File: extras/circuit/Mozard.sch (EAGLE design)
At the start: 44 parts, among them J4 Headphone/Line Out, U2 LM386

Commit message: Updated
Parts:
- C1: value 4.7nF -> 4.7nF/472
- C2: value 10uF -> 10uF/106
- C4: value 100nF -> 100nF/104
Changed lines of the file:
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@@
 <?xml version="1.0" encoding="utf-8"?>
 <!DOCTYPE eagle SYSTEM "eagle.dtd">
-<eagle version="9.1.1">
+<eagle version="9.1.3">
 <drawing>
 <settings>
@@
 <part name="VOLUME" library="SparkFun-Electromechanical" deviceset="POT" device="ALPS-KIT" value="VOLUME"/>
 <part name="R4" library="adafruit" deviceset="R-US_" device="0204/7" value="270"/>
-<part name="C4" library="SparkFun-Capacitors" deviceset="0.1UF-50V-20%(PTH)" device="KIT-EZ" value="100nF"/>
+<part name="C4" library="SparkFun-Capacitors" deviceset="0.1UF-50V-20%(PTH)" device="KIT-EZ" value="100nF/104"/>
 <part name="GND2" library="SparkFun-Aesthetics" deviceset="GND" device=""/>
 <part name="A7" library="SparkFun-Electromechanical" deviceset="POT" device="ALPS-KIT" value="A7"/>
@@
 <part name="P+1" library="supply1" library_urn="urn:adsk.eagle:library:371" deviceset="V+" device=""/>
 <part name="U$1" library="TOF" deviceset="NANO" device=""/>
-<part name="C1" library="SparkFun-Capacitors" deviceset="0.1UF-50V-20%(PTH)" device="KIT-EZ" value="4.7nF"/>
-<part name="C2" library="SparkFun-Capacitors" deviceset="0.1UF-50V-20%(PTH)" device="KIT-EZ" value="10uF"/>
+<part name="C1" library="SparkFun-Capacitors" deviceset="0.1UF-50V-20%(PTH)" device="KIT-EZ" value="4.7nF/472"/>
+<part name="C2" library="SparkFun-Capacitors" deviceset="0.1UF-50V-20%(PTH)" device="KIT-EZ" value="10uF/106"/>
 <part name="TOUCH1" library="TOF" deviceset="PCB-TOUCHPAD2" device=""/>
 <part name="GND3" library="SparkFun-Aesthetics" deviceset="GND" device=""/>

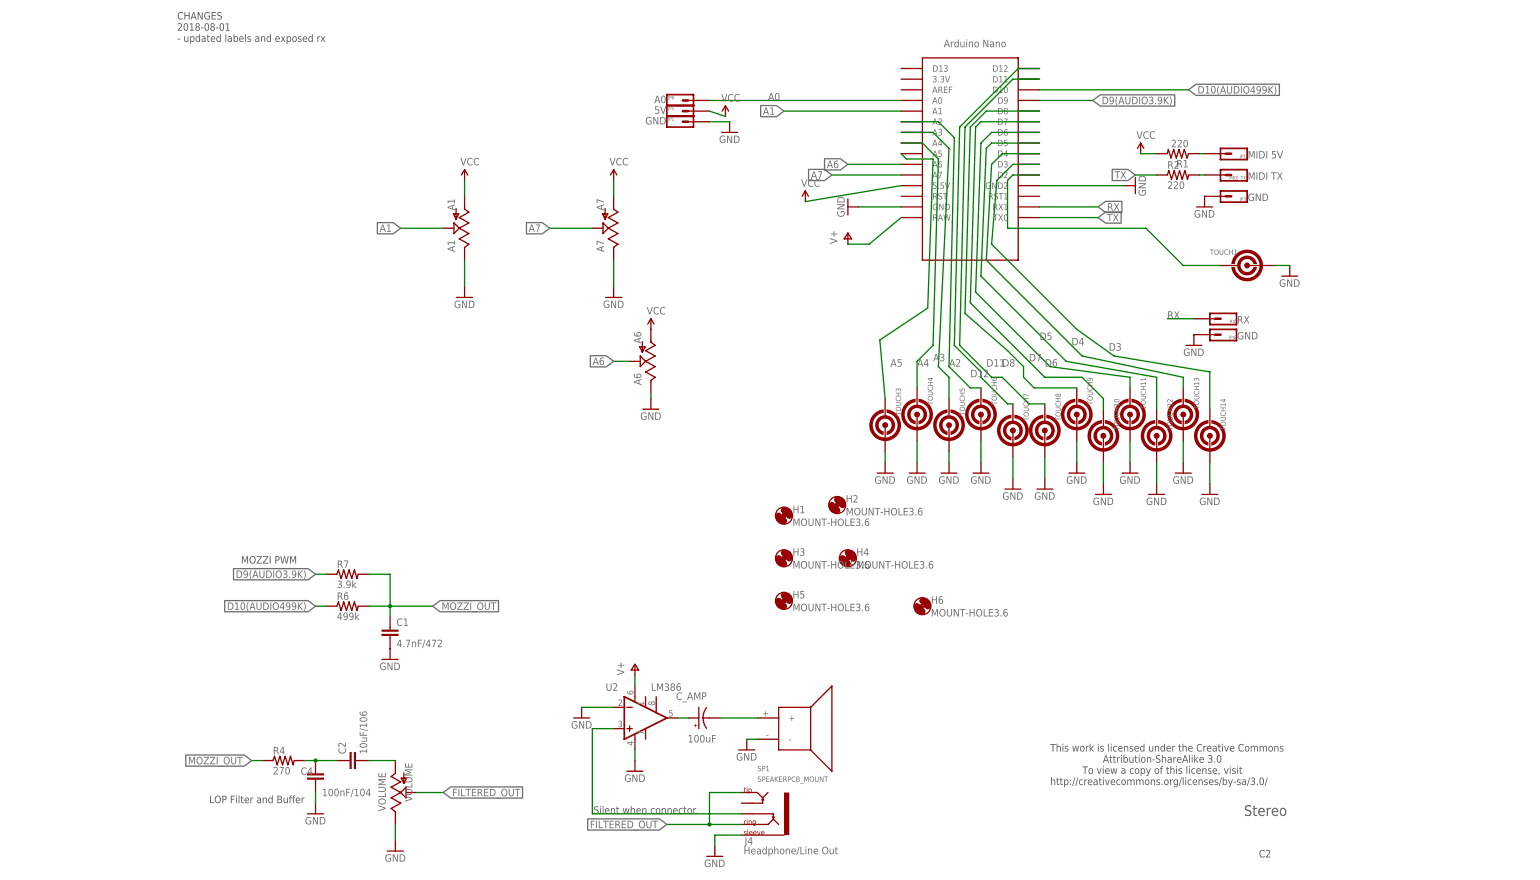
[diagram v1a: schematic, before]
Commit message: Fixed overlapping traces
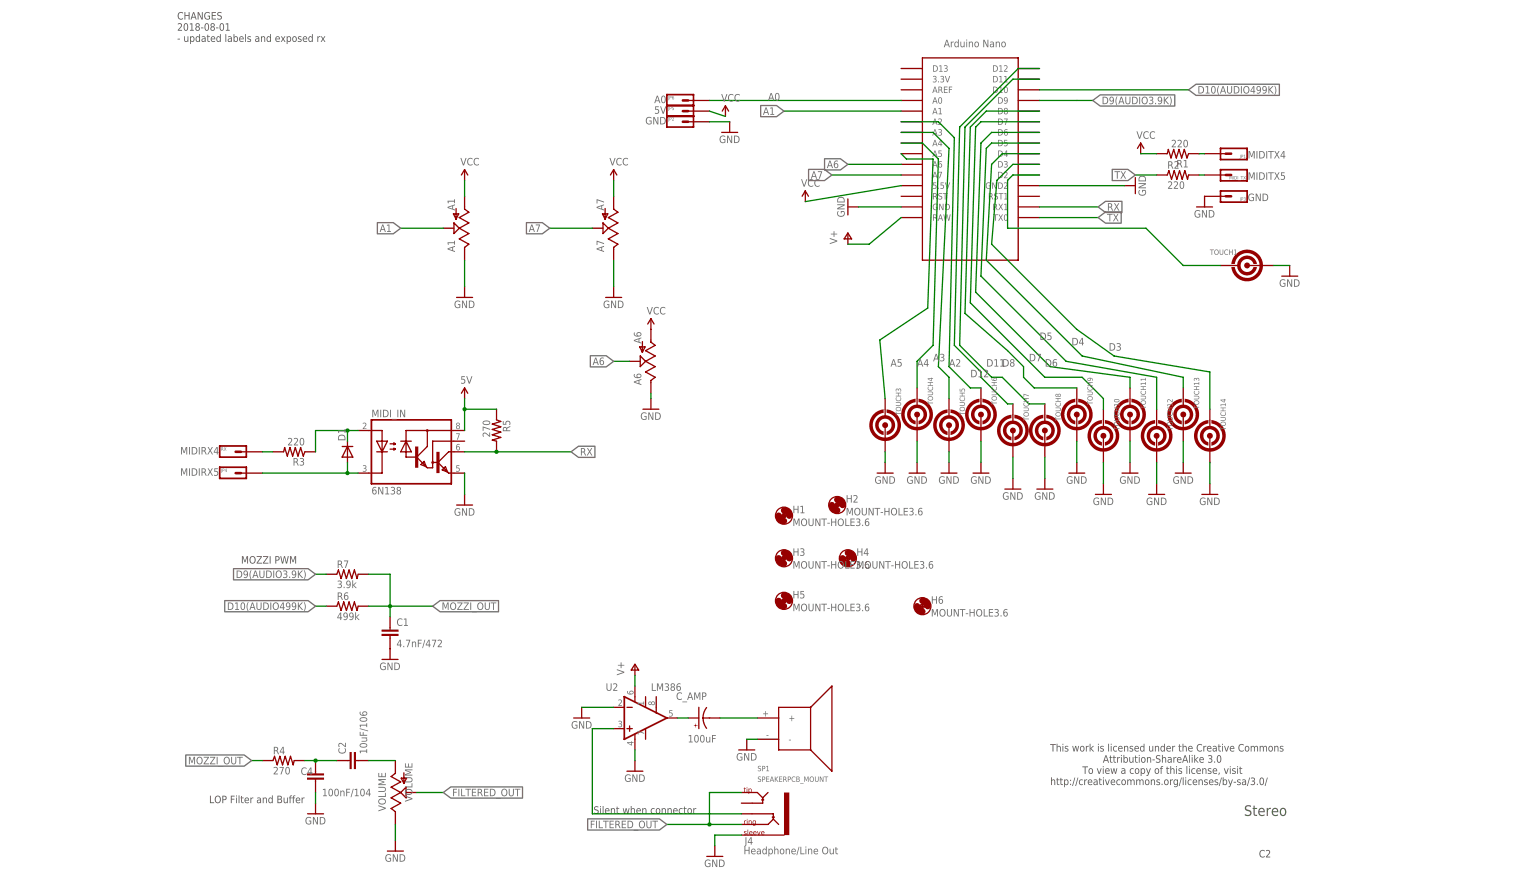
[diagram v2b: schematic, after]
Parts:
- added D1: 1N4148, adafruit:1N4004
- added MIDI_IN: 6N138, optocoupler:6N138
- added R3: 220, adafruit:R-US_0204/5
- added R5: 270, adafruit:R-US_0204/5
- JP1: value MIDI 5V -> MIDITX4
- JP4: value GND -> MIDIRX5
- MIDI_TX: value MIDI TX -> MIDITX5
- R1, R2: device adafruit:R-US_0204/7 -> adafruit:R-US_0204/5
- RX: value RX -> MIDIRX4
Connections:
- new net 5V: MIDI_IN.VCC, R5.1
- new net N$10: D1.C, MIDI_IN.A, R3.1
- new net N$8: D1.A, JP4.1, MIDI_IN.C
- new net N$9: R3.2, RX.1
- net GND: now also MIDI_IN.GND; no longer JP4.1
- net RX: now also MIDI_IN.VO, R5.2; no longer RX.1
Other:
- moved on the sheet: JP4, RX

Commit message: Sensitivity change
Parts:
- removed JP1: MIDITX4, TOF:HEADER-1X1
- removed JP3: GND, TOF:HEADER-1X1
- removed JP4: MIDIRX5, TOF:HEADER-1X1
- removed MIDI_TX: MIDITX5, TOF:HEADER-1X1
- removed R1, R2: 220, adafruit:R-US_0204/5
- removed RX: MIDIRX4, TOF:HEADER-1X1
- removed TOUCH1, TOUCH10, TOUCH11, TOUCH12, TOUCH13, TOUCH14, TOUCH3, TOUCH4, TOUCH5, TOUCH6, TOUCH7, TOUCH8, TOUCH9: (no value), TOF:PCB-TOUCHPAD2
- added MIDI_IN1: AUDIO-JACKKIT, TOF:AUDIO-JACKKIT
- added U$10, U$11, U$12, U$13, U$14, U$2, U$3, U$4, U$5, U$6, U$7, U$8, U$9: PCB-TOUCHPAD-1-PIN, TOF:PCB-TOUCHPAD-1-PIN
- A1, A6, A7, VOLUME: device SparkFun-Electromechanical:POTALPS-KIT -> TOF:POT
- D1: device adafruit:1N4004 -> TOF:DIODE
- MIDI_IN: device optocoupler:6N138 -> TOF:6N138
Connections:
- removed net N$3: JP1.1, R1.1
- removed net N$5: MIDI_TX.1, R2.2
- removed net N$8: D1.A, JP4.1, MIDI_IN.C
- removed net N$9: R3.2, RX.1
- new net M4: MIDI_IN1.RING, R3.2
- new net M5: D1.A, MIDI_IN.C, MIDI_IN1.TIP
- net A2: now also U$5.P$1; no longer TOUCH6.1
- net A3: now also U$4.P$1; no longer TOUCH5.1
- net A4: now also U$3.P$1; no longer TOUCH4.1
- net A5: now also U$2.P$1; no longer TOUCH3.1
- net D11: now also U$7.P$1; no longer TOUCH8.1
- net D12: now also U$6.P$1; no longer TOUCH7.1
- net D3: now also U$13.P$1; no longer TOUCH14.1
- net D4: now also U$12.P$1; no longer TOUCH13.1
- net D5: now also U$11.P$1; no longer TOUCH12.1
- net D6: now also U$10.P$1; no longer TOUCH11.1
- net D7: now also U$9.P$1; no longer TOUCH10.1
- net D8: now also U$8.P$1; no longer TOUCH9.1
- net GND: now also MIDI_IN1.SLEEVE; no longer JP3.1, TOUCH1.2, TOUCH10.2, TOUCH11.2, TOUCH12.2, TOUCH13.2, TOUCH14.2, TOUCH3.2, TOUCH4.2, TOUCH5.2, TOUCH6.2, TOUCH7.2, TOUCH8.2, TOUCH9.2
- net TOUCH_A: now also U$14.P$1; no longer TOUCH1.1
- net TX: no longer R2.1
- net VCC: no longer R1.2

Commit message: Cap removed, resistor added
Big capacitor removed because it was useless. 100k resistor added between + and - of amp to cancel noise when jack plugged in.
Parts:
- added R1: 100k, adafruit:R-US_0204/7
- C_AMP: device Mitch-parts:CPOL-RADIAL-10UF-25V -> TOF:CPOL-USE2.5-6
- SP1: value SPEAKERPCB_MOUNT -> SPEAKER
- renumbered D1 to 1N4148
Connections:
- net GND: now also R1.2
- net N$6: now also R1.1
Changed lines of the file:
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@@
 <setting verticaltext="up"/>
 </settings>
-<grid distance="0.1" unitdist="inch" unit="inch" style="lines" multiple="1" display="no" altdistance="0.025" altunitdist="inch" altunit="inch"/>
+<grid distance="0.1" unitdist="inch" unit="inch" style="lines" multiple="1" display="no" altdistance="0.01" altunitdist="inch" altunit="inch"/>
 <layers>
 <layer number="1" name="Top" color="4" fill="1" visible="no" active="no"/>
@@
 <part name="GND14" library="SparkFun-Aesthetics" deviceset="GND" device=""/>
 <part name="U2" library="Mitch-parts" deviceset="LM386" device=""/>
-<part name="C_AMP" library="Mitch-parts" deviceset="CPOL-RADIAL-10UF-25V" device="" value="100uF"/>
+<part name="C_AMP" library="TOF" deviceset="CPOL-US" device="E2.5-6" package3d_urn="urn:adsk.eagle:package:23349/1" value="100uF"/>
 <part name="P+1" library="supply1" library_urn="urn:adsk.eagle:library:371" deviceset="V+" device=""/>
 <part name="U$1" library="TOF" deviceset="NANO" device=""/>
@@
 <part name="H5" library="holes" library_urn="urn:adsk.eagle:library:237" deviceset="MOUNT-HOLE" device="3.6" package3d_urn="urn:adsk.eagle:package:14272/1"/>
 <part name="H6" library="holes" library_urn="urn:adsk.eagle:library:237" deviceset="MOUNT-HOLE" device="3.6" package3d_urn="urn:adsk.eagle:package:14272/1"/>
-<part name="SP1" library="SparkFun-Electromechanical" deviceset="SPEAKER" device="" technology="PCB_MOUNT"/>
+<part name="SP1" library="SparkFun-Electromechanical" deviceset="SPEAKER" device="" technology="PCB_MOUNT" value="SPEAKER"/>
 <part name="JP2" library="TOF" deviceset="HEADER-1X1" device="" value="GND"/>
 <part name="JP5" library="TOF" deviceset="HEADER-1X1" device="" value="5V"/>
@@
 <part name="SUPPLY5" library="SparkFun-Aesthetics" deviceset="VCC" device=""/>
 <part name="MIDI_IN" library="TOF" deviceset="6N138" device="" package3d_urn="urn:adsk.eagle:package:21941/1"/>
-<part name="D1" library="TOF" deviceset="DIODE" device="" value="1N4148"/>
+<part name="1N4148" library="TOF" deviceset="DIODE" device="" value="1N4148"/>
 <part name="R3" library="adafruit" deviceset="R-US_" device="0204/5" value="220"/>
 <part name="GND29" library="SparkFun-Aesthetics" deviceset="GND" device=""/>
@@
 <part name="U$13" library="TOF" deviceset="PCB-TOUCHPAD-1-PIN" device=""/>
 <part name="U$14" library="TOF" deviceset="PCB-TOUCHPAD-1-PIN" device=""/>
+<part name="R1" library="adafruit" deviceset="R-US_" device="0204/7" value="100k"/>
 </parts>
 <sheets>
@@
 <attribute name="VALUE" x="169.672" y="76.2762" size="1.778" layer="96"/>
 </instance>
-<instance part="GND4" gate="1" x="104.14" y="40.64" smashed="yes">
-<attribute name="VALUE" x="101.6" y="38.1" size="1.778" layer="96"/>
+<instance part="GND4" gate="1" x="88.9" y="40.64" smashed="yes">
+<attribute name="VALUE" x="86.36" y="38.1" size="1.778" layer="96"/>
 </instance>
 <instance part="GND14" gate="1" x="116.84" y="27.94" smashed="yes">
@@
 <attribute name="VALUE" x="53.975" y="93.98" size="1.778" layer="96"/>
 </instance>
-<instance part="D1" gate="1" x="48.26" y="104.14" smashed="yes" rot="R90">
+<instance part="1N4148" gate="1" x="48.26" y="104.14" smashed="yes" rot="R90">
 <attribute name="NAME" x="47.7774" y="106.68" size="1.778" layer="95" rot="R90"/>
 </instance>
@@
 <instance part="U$13" gate="G$1" x="254" y="106.68" smashed="yes" rot="R270"/>
 <instance part="U$14" gate="G$1" x="264.16" y="148.59" smashed="yes"/>
+<instance part="R1" gate="G$1" x="100.33" y="38.1" smashed="yes" rot="R90">
+<attribute name="NAME" x="98.8314" y="35.56" size="1.778" layer="95" rot="R90"/>
+<attribute name="VALUE" x="103.632" y="35.56" size="1.778" layer="96" rot="R90"/>
+</instance>
 </instances>
 <busses>
@@
 <segment>
 <pinref part="GND4" gate="1" pin="GND"/>
-<wire x1="111.76" y1="43.18" x2="104.14" y2="43.18" width="0.1524" layer="91"/>
+<wire x1="111.76" y1="43.18" x2="100.33" y2="43.18" width="0.1524" layer="91"/>
 <pinref part="U2" gate="G$1" pin="-IN"/>
+<pinref part="R1" gate="G$1" pin="2"/>
+<wire x1="100.33" y1="43.18" x2="88.9" y2="43.18" width="0.1524" layer="91"/>
+<junction x="100.33" y="43.18"/>
 </segment>
 <segment>
@@
 <pinref part="U2" gate="G$1" pin="+IN"/>
 <wire x1="111.76" y1="38.1" x2="106.68" y2="38.1" width="0.1524" layer="91"/>
-<wire x1="106.68" y1="38.1" x2="106.68" y2="17.78" width="0.1524" layer="91"/>
+<wire x1="106.68" y1="38.1" x2="106.68" y2="33.02" width="0.1524" layer="91"/>
+<wire x1="106.68" y1="33.02" x2="106.68" y2="17.78" width="0.1524" layer="91"/>
 <wire x1="106.68" y1="17.78" x2="142.24" y2="17.78" width="0.1524" layer="91"/>
 <pinref part="J4" gate="G$1" pin="RSH"/>
+<pinref part="R1" gate="G$1" pin="1"/>
+<wire x1="100.33" y1="33.02" x2="106.68" y2="33.02" width="0.1524" layer="91"/>
+<junction x="106.68" y="33.02"/>
 </segment>
 </net>
@@
 <pinref part="MIDI_IN" gate="G$1" pin="A"/>
 <wire x1="40.64" y1="109.22" x2="48.26" y2="109.22" width="0.1524" layer="91"/>
-<pinref part="D1" gate="1" pin="C"/>
+<pinref part="1N4148" gate="1" pin="C"/>
 <wire x1="48.26" y1="109.22" x2="50.8" y2="109.22" width="0.1524" layer="91"/>
 <wire x1="48.26" y1="106.68" x2="48.26" y2="109.22" width="0.1524" layer="91"/>
@@
 <pinref part="MIDI_IN" gate="G$1" pin="C"/>
 <wire x1="27.94" y1="99.06" x2="48.26" y2="99.06" width="0.1524" layer="91"/>
-<pinref part="D1" gate="1" pin="A"/>
+<pinref part="1N4148" gate="1" pin="A"/>
 <wire x1="48.26" y1="99.06" x2="50.8" y2="99.06" width="0.1524" layer="91"/>
 <wire x1="48.26" y1="101.6" x2="48.26" y2="99.06" width="0.1524" layer="91"/>
@@
 packages will not be understood (or retained) with this version.
 </note>
+<note version="8.4" severity="warning">
+Since Version 8.4, EAGLE supports properties for SPICE simulation.
+Probes in schematics and SPICE mapping objects found in parts and library devices
+will not be understood with this version. Update EAGLE to the latest version
+for full support of SPICE simulation.
+</note>
 </compatibility>
